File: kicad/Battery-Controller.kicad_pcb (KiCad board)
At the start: 2 copper layers, 59 parts, among them J1 Screw_Terminal_01x04 - RELAY, J2 Screw_Terminal_01x04 - COM, J3 Screw_Terminal_01x06 - RELAY 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, J4 Screw_Terminal_01x02 - Batter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, J5 Screw_Terminal_01x02 - SOC En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, J6 Screw_Terminal_01x04 - Cells, J7 Conn_01x15_Male, J8 Conn_01x15_Female, Q1 TIP120, Q2 IRFZ44N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

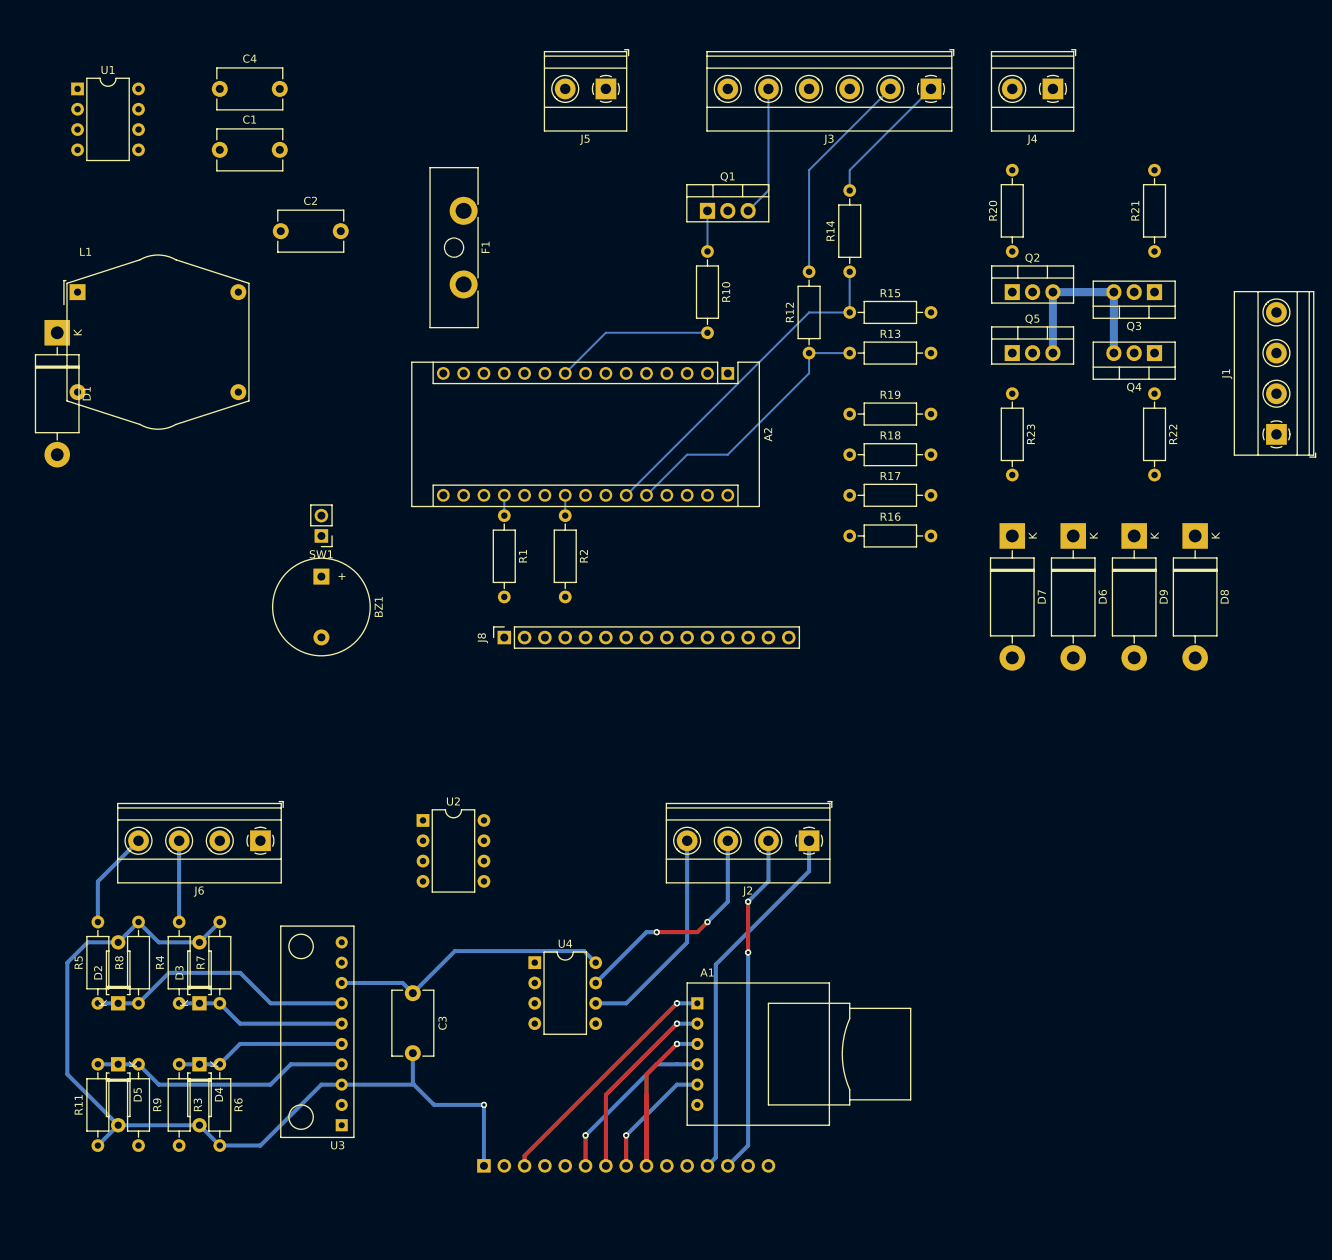
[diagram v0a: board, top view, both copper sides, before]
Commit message: Ajout logs SD Card
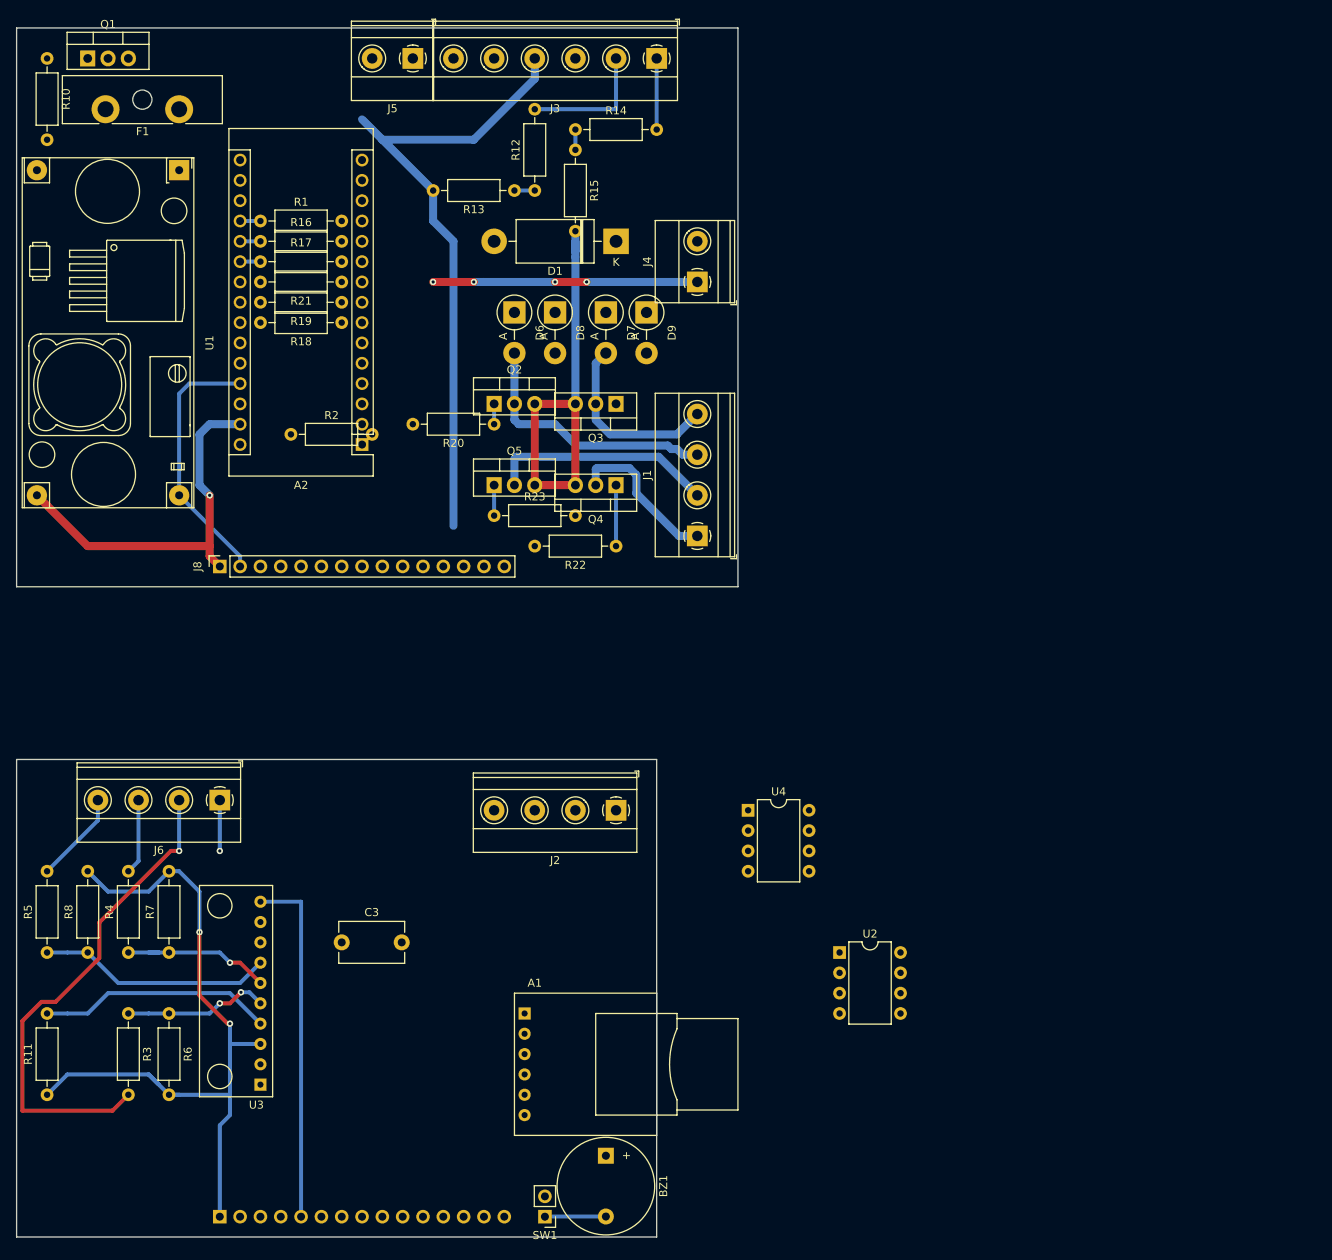
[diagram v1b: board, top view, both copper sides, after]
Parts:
- removed C1, C4: 100uF, Capacitor_THT:C_Disc_D8.0mm_W5.0mm_P7.50mm
- removed C2: 10nF, Capacitor_THT:C_Disc_D8.0mm_W5.0mm_P7.50mm
- removed D2, D3, D4, D5: 4.7V, Diode_THT:D_A-405_P7.62mm_Horizontal
- removed L1: 100uH, Inductor_THT:Choke_Schaffner_RN116-04-22.5x21.5mm
- removed R9: 100, Resistor_THT:R_Axial_DIN0207_L6.3mm_D2.5mm_P10.16mm_Horizontal
- D6, D7, D8, D9: footprint Diode_THT:D_DO-201AD_P15.24mm_Horizontal -> Diode_THT:D_5W_P5.08mm_Vertical_AnodeUp
- R3: value 2.2K -> 21.6K
- R4: value 10K -> 474
- R5: value 2.2K -> 5.1K
- R6: value 2K -> 32K
- R7: value 5.6K -> 330
- R8: value 1K -> 2.2K
- U1: value LM2674N-5.0 -> YAAJ_DCDC_StepDown_LM2596; footprint Package_DIP:DIP-8_W7.62mm -> DC_DC_LM2596:YAAJ_DCDC_StepDown_LM2596
- moved R21 101.7 mm to (101.6, 67.3), turned to 180 degrees
- moved SW1 89.6 mm to (127.0, 184.2)
- moved R10 86.0 mm to (64.8, 39.4)
- moved D8 84.7 mm to (128.3, 71.1)
- moved R16 82.4 mm to (91.4, 62.2)
- moved BZ1 80.7 mm to (134.6, 176.5)
- moved Q1 79.8 mm to (69.8, 39.4)
- moved R17 79.2 mm to (91.4, 64.8)
- moved D6 75.2 mm to (123.2, 71.1)
- moved J1 73.5 mm to (146.1, 99.1)
- moved D1 70.8 mm to (135.9, 62.2), turned to 180 degrees
- moved R22 70.0 mm to (135.9, 100.3), turned to 180 degrees
- moved Q4 69.3 mm to (135.9, 92.7)
- moved Q3 68.7 mm to (135.9, 82.5)
- moved R20 68.3 mm to (120.7, 85.1), turned to 180 degrees
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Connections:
- A1 pad 1: TUP-02 -> UP-3.3V
- A2 pad 1: Net-(A2-Pad1) -> (no net)
- A2 pad 18: Net-(A2-Pad18) -> (no net)
- A2 pad 2: Net-(A2-Pad2) -> (no net)
- A2 pad 28: Net-(A2-Pad28) -> (no net)
- A2 pad 3: Net-(A2-Pad3) -> (no net)
- A2 pad 30: Net-(A2-Pad30) -> (no net)
- A2 pad 4: Net-(A2-Pad4) -> (no net)
- BZ1 pad 1: BAT-GND -> TUP-01
- C3 pad 1: +5V -> UP-5V
- D1 pad 2: BAT-GND -> BAT-12V
- D6 pad 1: CHARGE-RELAY-ON -> BAT-12V
- D6 pad 2: BAT-GND -> CHARGE-RELAY-ON
- D7 pad 1: CHARGE-RELAY-OFF -> BAT-12V
- D7 pad 2: BAT-GND -> CHARGE-RELAY-OFF
- D8 pad 1: LOAD-RELAY-ON -> BAT-12V
- D8 pad 2: BAT-GND -> LOAD-RELAY-ON
- D9 pad 1: LOAD-RELAY-OFF -> BAT-12V
- D9 pad 2: BAT-GND -> LOAD-RELAY-OFF
- J3 pad 6: Net-(J3-Pad6) -> (no net)
- J7 pad 12: VICTRON-IN-1 -> UP-D7
- J7 pad 13: VICTRON-IN-2 -> VICTRON-IN-1
- J7 pad 14: Net-(J7-Pad14) -> VICTRON-IN-2
- J7 pad 15: Net-(J7-Pad15) -> (no net)
- J7 pad 2: TUP-02 -> UP-5V
- J7 pad 3: TUP-02 -> UP-3.3V
- J8 pad 12: D8 -> D7
- J8 pad 13: D9 -> D8
- J8 pad 14: Net-(J8-Pad14) -> D9
- J8 pad 15: Net-(J8-Pad15) -> (no net)
- J8 pad 2: +5V -> 5V
- R11 pad 2: Net-(D5-Pad1) -> CELL-1
- SW1 pad 2: D7 -> UP-D7
- U1 pad 1: Net-(C2-Pad2) -> Net-(D1-Pad1)
- U1 pad 2: Net-(U1-Pad2) -> BAT-GND
- U1 pad 3: Net-(U1-Pad3) -> BAT-GND
- U1 pad 4: +5V -> 5V
- U2 pad 1: Net-(U2-Pad1) -> (no net)
- U2 pad 2: Net-(U2-Pad2) -> (no net)
- U2 pad 3: Net-(U2-Pad3) -> UP-5V
- U2 pad 7: Net-(U2-Pad7) -> (no net)
- U2 pad 8: TUP-02 -> (no net)
- U3 pad 1: Net-(U3-Pad1) -> (no net)
- U3 pad 2: Net-(U3-Pad2) -> (no net)
- U3 pad 4: Net-(D5-Pad1) -> CELL-1
- U3 pad 8: +5V -> UP-5V
- U4 pad 2: Net-(U4-Pad2) -> (no net)
- U4 pad 3: Net-(U4-Pad3) -> (no net)
- U4 pad 5: BAT-GND -> TUP-01
- U4 pad 8: +5V -> UP-5V
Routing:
- net BAT-GND: track 26.4 -> 181.0 mm, vias 0 -> 1
- net CELL-2: track 0.00 -> 62.6 mm, vias 0 -> 1
- net VICTRON-IN-1: track 45.9 -> 0.00 mm
- net UP-SCL: track 0.00 -> 44.5 mm
- net VICTRON-IN-2: track 42.7 -> 0.00 mm, vias 2 -> 0
- net A6: track 42.5 -> 2.54 mm
- net CELL-1: track 0.00 -> 35.7 mm, vias 0 -> 1
- net +5V: track 35.1 -> 0.00 mm
- net BAT-12V: track 0.00 -> 33.0 mm, vias 0 -> 4
- net CHARGE-RELAY-ON: track 0.00 -> 33.0 mm
- net 5V: track 0.00 -> 32.9 mm
- net Net-(D5-Pad1): track 32.6 -> 0.00 mm
- net A7: track 34.3 -> 2.54 mm
- net TUP-02: track 31.1 -> 0.00 mm, vias 1 -> 0
- net RS-485-OUT1: track 28.3 -> 0.00 mm, vias 2 -> 0
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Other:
- board outline added: 90.2 x 151.1 mm

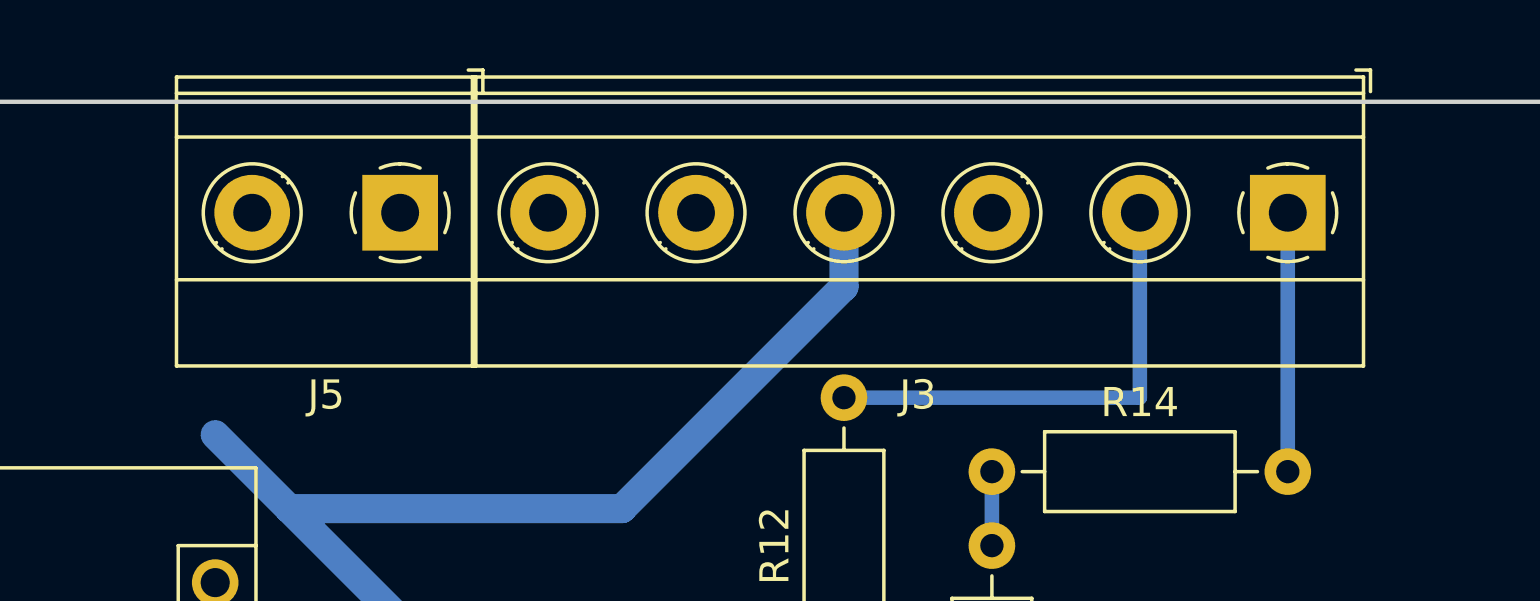
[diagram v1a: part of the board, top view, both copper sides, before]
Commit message: Intégration des routines de surveillance de la température
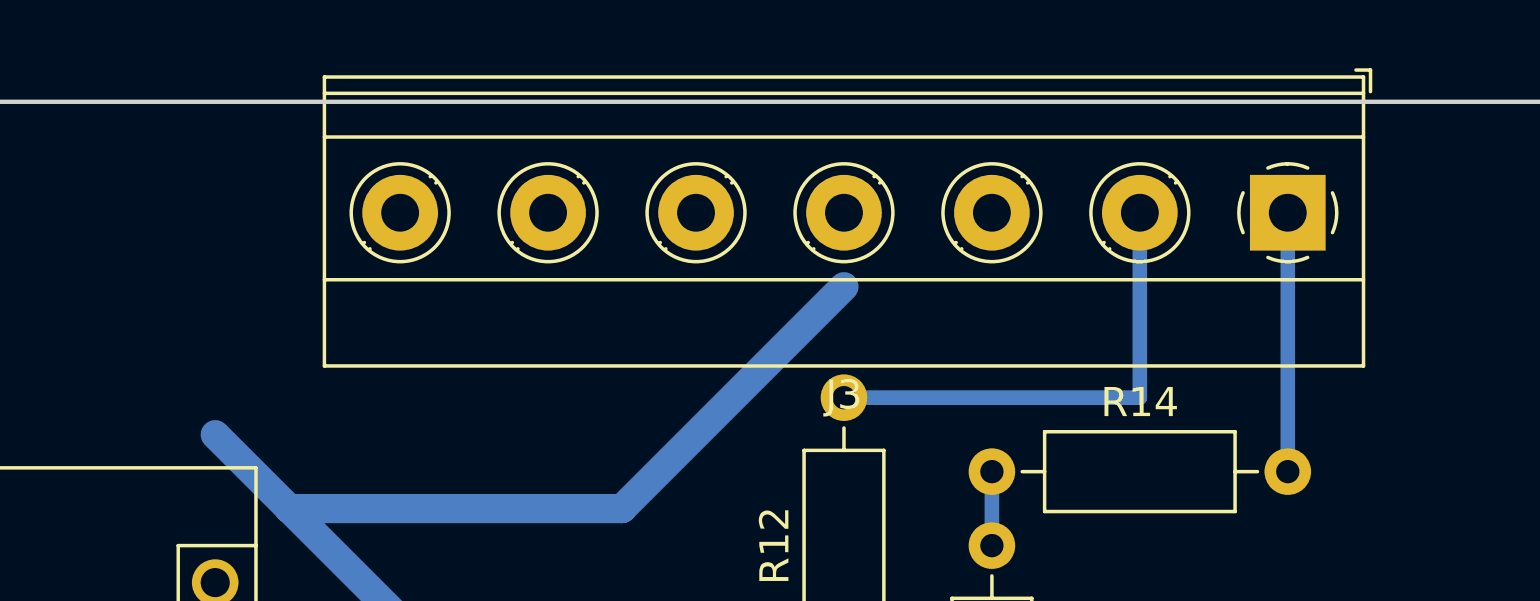
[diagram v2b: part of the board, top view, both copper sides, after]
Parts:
- removed J5: Screw_Terminal_01x02 - SOC Enable, TerminalBlock_Phoenix:TerminalBlock_Phoenix_MKDS-1,5-2-5.08_1x02_P5.08mm_Horizontal
- J3: value Screw_Terminal_01x06 - RELAY STATUS -> Screw_Terminal_01x08 - RELAY STATUS; footprint TerminalBlock_Phoenix:TerminalBlock_Phoenix_MKDS-1,5-6-5.08_1x06_P5.08mm_Horizontal -> TerminalBlock_Phoenix:TerminalBlock_Phoenix_MKDS-1,5-7-5.08_1x07_P5.08mm_Horizontal
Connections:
- J3 pad 3: A0 -> BAT-GND
- J3 pad 4: BAT-GND -> A0
- J3 pad 6: (no net) -> 5V
- R1 pad 2: +5V -> 3.3V
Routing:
- net BAT-GND: track 181.0 -> 178.5 mm

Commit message: Optimisation du code
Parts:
- removed D7, D8, D9: 1N5822, Diode_THT:D_5W_P5.08mm_Vertical_AnodeUp
- removed R21, R22, R23: 47, Resistor_THT:R_Axial_DIN0207_L6.3mm_D2.5mm_P10.16mm_Horizontal
- added D2: 1N5822, Diode_THT:D_5W_P5.08mm_Vertical_AnodeUp, F.Cu at (204.2, 55.6)
- added D3: 1N5822, Diode_THT:D_5W_P5.08mm_Vertical_AnodeUp, F.Cu at (204.2, 61.0)
- added D4: 1N5822, Diode_THT:D_5W_P5.08mm_Vertical_AnodeUp, F.Cu at (202.5, 67.5)
- added Q6: TIP42C, Package_TO_SOT_THT:TO-220-3_Vertical, F.Cu at (132.1, 96.5)
- added Q7: TIP42C, Package_TO_SOT_THT:TO-220-3_Vertical, F.Cu at (132.1, 90.2)
- added Q8: TIP42C, Package_TO_SOT_THT:TO-220-3_Vertical, F.Cu at (132.1, 83.8)
- added Q9: TIP42C, Package_TO_SOT_THT:TO-220-3_Vertical, F.Cu at (132.1, 77.5)
- added R9: 10K, Resistor_THT:R_Axial_DIN0207_L6.3mm_D2.5mm_P10.16mm_Horizontal, F.Cu at (137.2, 57.1)
- J3: value Screw_Terminal_01x08 - RELAY STATUS -> Screw_Terminal_01x08; footprint TerminalBlock_Phoenix:TerminalBlock_Phoenix_MKDS-1,5-7-5.08_1x07_P5.08mm_Horizontal -> TerminalBlock_Phoenix:TerminalBlock_Phoenix_MKDS-1,5-8-5.08_1x08_P5.08mm_Horizontal
- Q2, Q3, Q4, Q5: value IRFZ44N -> TIP122
- R12, R16, R17, R18, R19: value 10K -> 1K
- R13, R15: value 4.7K -> 1K
- R20: value 47 -> 1K
- moved D6 49.4 mm to (158.8, 36.8)
- moved R17 44.7 mm to (128.3, 90.2), turned to 180 degrees
- moved D1 43.0 mm to (176.5, 48.3)
- moved R16 42.4 mm to (118.1, 95.2)
- moved R12 37.4 mm to (114.3, 91.4)
- moved Q2 36.9 mm to (118.1, 119.4)
- moved Q3 35.3 mm to (118.1, 113.0), turned to 0 degrees
- moved Q5 33.3 mm to (146.1, 114.3)
- moved R15 31.4 mm to (114.3, 77.5), turned to 90 degrees
- moved R13 29.5 mm to (110.5, 82.5), turned to 90 degrees
- moved R2 26.9 mm to (99.1, 113.0)
- moved Q4 21.6 mm to (134.6, 114.3), turned to 0 degrees
- moved R18 20.1 mm to (118.1, 83.8), turned to 0 degrees
- moved R19 18.2 mm to (118.1, 77.5), turned to 0 degrees
- moved R20 18.1 mm to (109.2, 99.1), turned to 90 degrees
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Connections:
- D1 pad 2: BAT-12V -> (no net)
- D6 pad 1: BAT-12V -> CHARGE-RELAY-ON
- D6 pad 2: CHARGE-RELAY-ON -> BAT-12V
- J1 pad 1: LOAD-RELAY-ON -> CHARGE-RELAY-ON
- J1 pad 2: LOAD-RELAY-OFF -> CHARGE-RELAY-OFF
- J1 pad 3: CHARGE-RELAY-ON -> LOAD-RELAY-ON
- J1 pad 4: CHARGE-RELAY-OFF -> LOAD-RELAY-OFF
- J3 pad 1: CHARGE-RELAY-STATUS -> A6
- J3 pad 2: LOAD-RELAY-STATUS -> A7
- Q2 pad 2: CHARGE-RELAY-ON -> Net-(Q2-Pad2)
- Q3 pad 2: CHARGE-RELAY-OFF -> Net-(Q3-Pad2)
- Q4 pad 2: LOAD-RELAY-ON -> Net-(Q4-Pad2)
- Q5 pad 2: LOAD-RELAY-OFF -> Net-(Q5-Pad2)
- R12 pad 1: A7 -> Net-(Q3-Pad1)
- R12 pad 2: LOAD-RELAY-STATUS -> A2
- R13 pad 1: A7 -> Net-(Q4-Pad1)
- R13 pad 2: BAT-GND -> D4
- R14 pad 1: A6 -> 5V
- R14 pad 2: CHARGE-RELAY-STATUS -> A6
- R15 pad 1: A6 -> Net-(Q5-Pad1)
- R15 pad 2: BAT-GND -> D5
- R16 pad 1: A1 -> BAT-12V
- R16 pad 2: BAT-GND -> Net-(Q2-Pad2)
- R17 pad 1: A2 -> BAT-12V
- R17 pad 2: BAT-GND -> Net-(Q3-Pad2)
- R18 pad 1: D4 -> BAT-12V
- R18 pad 2: BAT-GND -> Net-(Q4-Pad2)
- R19 pad 1: D5 -> BAT-12V
- R19 pad 2: BAT-GND -> Net-(Q5-Pad2)
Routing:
- net BAT-GND: track 178.5 -> 47.4 mm
- net BAT-12V: track 33.0 -> 0.00 mm, vias 4 -> 0
- net CHARGE-RELAY-ON: track 33.0 -> 0.00 mm
- net LOAD-RELAY-OFF: track 28.3 -> 0.00 mm
- net CHARGE-RELAY-OFF: track 23.4 -> 0.00 mm
- net LOAD-RELAY-ON: track 19.6 -> 0.00 mm
- net LOAD-RELAY-STATUS: track 16.5 -> 0.00 mm
- net CHARGE-RELAY-STATUS: track 8.89 -> 0.00 mm
- net Net-(Q4-Pad1): track 7.62 -> 0.00 mm
- net Net-(Q5-Pad1): track 3.81 -> 0.00 mm
- net Net-(Q2-Pad1): track 2.54 -> 0.00 mm
- net A7: track 2.54 -> 0.00 mm
- net A6: track 2.54 -> 0.00 mm
- net A1: track 2.54 -> 0.00 mm
